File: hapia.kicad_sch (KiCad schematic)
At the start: 61 parts, among them CN1 100nf, CN2 100nf, J1 USB_C_Receptacle_USB2.0_16P, J18 Conn_ARM_JTAG_SWD_10, SW1 SW_Push, SW2 SW_Push, U1 AMS1117-3.3, U2 STM32F407VET6, U3 SRV05-4, Y1 8mhz

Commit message: 21082026/G
falta muita coisa
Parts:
- removed R10, R9: 33Ω, symbol Device:R
- removed R11: 1kΩ, symbol Device:R
- removed unit 2 of RN1
- removed unit 1 of RN1
- removed unit 6 of RN1
- removed unit 3 of RN1
- removed unit 5 of RN1
- removed unit 7 of RN1
- removed unit 4 of RN1
- removed unit 4 of RN2
- removed unit 1 of RN2
- removed unit 5 of RN2
- removed unit 6 of RN2
- removed unit 2 of RN2
- removed unit 3 of RN2
- removed unit 8 of RN2
- removed unit 3 of RN3
- removed unit 5 of RN3
- removed unit 7 of RN3
- removed unit 6 of RN3
- removed unit 1 of RN3
- removed unit 4 of RN3
- added R14, R15, R16, R17, R18, R19, R2, R20, R21, R22, R23, R24, R25, R26, R3, R30, R31, R32, R33, R34, R35, R36, R37, R38, R39, R40, R45, R46, R47, R5, R6, R7: 33Ω, symbol Device:R
- renumbered C16 to C10, C14 to C11, C17 to C12, C13 to C2, C2 to C3, C3 to C4, C11 to C5, C67 to C6, C4 to C7, C29 to C8, C5 to C9, D5 to D1, D1 to D2, FB2 to FB1, J18 to J1, J1 to J2, R43 to R1, R6 to R10, R24 to R11, R25 to R12, R4 to R13, R42 to R27, R23 to R28, R22 to R29, R3 to R4, R12 to R41, R13 to R42, R14 to R43, R5 to R44, R15 to R48, R16 to R49, R18 to R50, R19 to R51, R1 to R52, R20 to R53, R21 to R54, R7 to R9, RN3 to RN1, RN2 to RN1, RN1 to RN2, RN4 to RN3, RN5 to RN4, TP12 to TP1, TP16 to TP2, TP1 to TP3, TP2 to TP4, U2 to U1, U1 to U2
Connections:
- net Fan_1: now also R16.2; no longer R8.2
- net NTC_MUX_0: now also U1.55 (PD8); no longer U1.42 (PE11)
- net NTC_MUX_1: now also U1.56 (PD9); no longer U1.43 (PE12)
- net NTC_MUX_2: now also U1.57 (PD10); no longer U1.44 (PE13)
- net NTC_MUX_out: now also U1.15 (PC0); no longer U1.41 (PE10)
- net SUB_2: now also R33.2
- net SUB_3: now also R34.2
- net SUB_4: now also R35.2
- net SUB_5: now also R36.2
- net SUB_6: now also RN2.9 (R8.2)
- net SUB_SCL: now also R4.2
- net SUB_SDA: now also R5.2; no longer RN1.15 (R2.2)
- net SUB_led: now also R6.2; no longer RN2.9 (R8.2)
- net SWD_SWO: now also U1.35 (PB0); no longer U1.89 (PB3)
- net SWD/jtag_rst: now also U1.36 (PB1); no longer U1.90 (PB4)
- net TMC_DIR_3: now also R9.2; no longer RN4.3 (R3.1)
- net TMC_step_3: now also R10.2, R8.2; no longer RN4.2 (R2.1), RN4.4 (R4.1)
- net USB_C_D+: now also R26.2; no longer RN1.9 (R8.2)
- net USB_C_D-: now also R25.2; no longer RN1.10 (R7.2)
- net cont_sd: now also R7.2; no longer R4.2
- net exrtusora: now also R14.2; no longer R10.2
- net gpi_PD0: now also R45.2
- net gpi_PD1: now also R47.2
- net gpi_PD10: now also R24.2
- net gpi_PD11: now also R30.2
- net gpi_PD12: now also R31.2
- net gpi_PD13: now also R32.2
- net gpi_PD14: now also R2.2
- net gpi_PD15: now also R3.2
- net gpi_PD2: now also R46.2
- net gpi_PD3: now also R17.2
- net gpi_PD4: now also R18.2
- net gpi_PD5: now also R19.2
- net gpi_PD6: now also R20.2
- net gpi_PD7: now also R21.2
- net gpi_PD8: now also R22.2
- net gpi_PD9: now also R23.2
- net hot_bed: now also R15.2; no longer R9.2
- net at U1.82 (PD1): now also R18.1
- net at U1.81 (PD0): now also R17.1
- net at R13.1: now also U1.43 (PE12); no longer U1.40 (PE9)
- net at R43.1: now also U1.65 (PC8); no longer U1.80 (PC12)
- net at U1.91 (PB5): now also R32.1
- net at R8.1: now also U1.38 (PE7); no longer U1.37 (PB2)
- net at U1.86 (PD5): now also R22.1
- net at U1.64 (PC7): now also R42.1
- net at U1.93 (PB7): now also R34.1
- net at U1.1 (PE2): now also RN2.8 (R8.1)
- net at U1.17 (PC2): now also R39.1
- net at U1.18 (PC3): now also R40.1
- net at U1.2 (PE3): now also R4.1
- net at U1.3 (PE4): now also R5.1
- net at R10.1: now also U1.40 (PE9); no longer U1.35 (PB0)
- net at R9.1: now also U1.39 (PE8); no longer U1.36 (PB1)
- net at R11.1: now also U1.41 (PE10); no longer U1.38 (PE7)
- net at R12.1: now also U1.42 (PE11); no longer U1.39 (PE8)
- net at U1.4 (PE5): now also R6.1
- net at U1.45 (PE14): now also R15.1
- net at U1.46 (PE15): now also R16.1
- net at U1.5 (PE6): now also R7.1
- net at U1.51 (PB12): now also R37.1
- net at U1.52 (PB13): now also R38.1
- net at U1.61 (PD14): now also R25.1; no longer RN1.7 (R7.1)
- net at U1.62 (PD15): now also R26.1; no longer RN1.8 (R8.1)
- net at U1.63 (PC6): now also R41.1
- net at U1.66 (PC9): now also R44.1
- net at U1.77 (PA15): no longer R44.1
- net at U1.78 (PC10): now also R45.1; no longer R41.1
- net at U1.79 (PC11): now also R46.1; no longer R42.1
- net at U1.83 (PD2): now also R19.1
- net at U1.84 (PD3): now also R20.1
- net at U1.85 (PD4): now also R21.1
- net at U1.87 (PD6): now also R23.1
- net at U1.88 (PD7): now also R24.1
- net at U1.92 (PB6): now also R33.1
- net at U1.95 (PB8): now also R35.1
- net at U1.96 (PB9): now also R36.1
- net at U1.97 (PE0): now also R2.1; no longer RN2.8 (R8.1)
- net at U1.98 (PE1): now also R3.1; no longer R4.1
- new net: R30.1, U1.89 (PB3)
- new net: R14.1, U1.44 (PE13)
- new net: R47.1, U1.80 (PC12)
- new net: R31.1, U1.90 (PB4)
- new net SUB_GPIO_1: R39.2
- new net SUB_GPIO_2: R40.2
- new net SUB_RMII_CRS_DV: RN4.2 (R2.1)
- new net SUB_RMII_RXD0: RN4.3 (R3.1)
- new net SUB_RMII_RXD1: RN4.4 (R4.1)
- new net SUB_RMII_TXD0: R37.2
- new net SUB_RMII_TXD1: R38.2
- new net SUB_RMII_TXEN: RN1.15 (R2.2)
- no-connect marks 31 -> 23
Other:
- moved on the sheet: R10, R11, R12, R13, R4, R41, R42, R43, R44, R49, R8, R9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

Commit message: 23082026/H
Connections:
- net ATX_PWR_o: now reaches U1.47 (PB10)
- no-connect marks 23 -> 22
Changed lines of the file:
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@@
-	)
-	(no_connect
-		(at 128.27 163.83)
 	)
 	(no_connect
@@
 			(hide yes)
 			(show_name no)
+			(do_not_autoplace no)
+			(effects
+				(font
+					(size 1.27 1.27)
+				)
+				(justify left)
+			)
+		)
+	)
+	(global_label "ATX_PWR_o"
+		(shape input)
+		(at 128.27 163.83 0)
+		(fields_autoplaced yes)
+		(effects
+			(font
+				(size 1.27 1.27)
+			)
+			(justify left)
+		)
+		(property "Intersheetrefs" "${INTERSHEET_REFS}"
+			(at 141.5965 163.83 0)
+			(hide yes)
+			(show_name no)

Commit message: 29082026/I
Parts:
- removed R10, R11, R12, R13, R14, R15, R16, R17, R18, R19, R2, R20, R21, R22, R23, R24, R3, R36, R37, R38, R39, R4, R44, R45, R46, R47, R5, R6, R7, R8, R9: 33Ω, symbol Device:R
- removed R43: 33r, symbol Device:R
- removed unit 2 of RN1
- removed RN3, RN4: 33Ω, Resistor_SMD:R_Array_Convex_4x0603, symbol Device:R_Pack04_Split
- added R110, R111, R112, R113, R75: 33Ω, symbol Device:R
- added unit 4 of RN1
- added unit 6 of RN1
- added unit 3 of RN1
- added unit 5 of RN1
- added unit 4 of RN2
- added unit 6 of RN2
- added unit 1 of RN2
- added unit 2 of RN2
- added unit 3 of RN2
- added unit 7 of RN2
- added unit 5 of RN2
- added RN4: 33Ω, symbol Device:R_Pack08_Split
- added RN5, RN6: 33Ω, Resistor_SMD:R_Array_Concave_4x0402, symbol Device:R_Pack04_Split
- C10: footprint (none) -> Capacitor_SMD:C_0603_1608Metric; jlc_pcb: (none) -> C162274; mouser: (none) -> 81-GRM188R61E475KE1D; mpn (none) -> GRM188R61E475KE11D
- C11, C2: footprint (none) -> Capacitor_SMD:C_1206_3216Metric_Pad1.33x1.80mm_HandSolder; jlc_pcb: (none) -> C13585; mouser: (none) -> 187-CL31B106KLK6PNE; mpn (none) -> CL31A106KBHNNNE
- C3, C4, C7, C9: jlc_pcb: C346191 -> C307348; mouser: (none) -> 187-CL10B104KB8WPNC; mpn CL10B104KB8NFNC -> CL10B104KB8WPNC
- C6: footprint (none) -> Capacitor_SMD:C_1206_3216Metric_Pad1.33x1.80mm_HandSolder; Descrição (none) -> esse capacitor e conectado entre o gnd e o vcc(VDDA) do ci 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; jlc_pcb: (none) -> C13585; mouser: (none) -> 187-CL31B106KLK6PNE; mpn (none) -> CL31A106KBHNNNE
- C8: footprint (none) -> Capacitor_SMD:C_0603_1608Metric; Descrição (none) -> capacitor ceramico 4.7uf(µf); jlc_pcb: (none) -> C162274; mouser: (none) -> 81-GRM188R61E475KE1D; mpn (none) -> GRM188R61E475KE11D
- CN1, CN2: jlc_pcb: C346191 -> C307348; mouser: (none) -> 187-CL10B104KB8WPNC; mpn CA0612MRX7R7BB104 -> CL10B104KB8WPNC
- J2: footprint (none) -> Connector_USB:USB_C_Receptacle_HCTL_HC-TYPE-C-16P-01A; jlc_pcb: (none) -> C5150972; mouser: (none) -> 523-12402012E212A; mpn (none) -> 12402012E212A
- R25, R26: value 33Ω -> 22Ω
- R41, R42: value 33r -> 33Ω
- R48: value 1k -> 1kΩ
- RN1, RN2: footprint Resistor_SMD:R_Array_Convex_8x0602 -> (none)
- U1: mouser: (none) -> 511-STM32F407VET6
- U2: mouser: (none) -> 926-LM1117MPX3.3NOPB
- Y1: mouser: (none) -> 815-ABM3-8-D2Y-T
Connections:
- net ATX_PWR_o: now also RN1.8 (R8.1); no longer U1.47 (PB10)
- net Fan_1: now also RN6.5 (R4.2)
- net Fan_2: now also RN6.8 (R1.2)
- net SDW_SWCLK: now also R41.2; no longer R29.2
- net SDW_SWDIO: now also R40.2; no longer R28.2
- net SUB_2: now also RN1.6 (R6.1); no longer R33.2
- net SUB_3: now also RN1.5 (R5.1); no longer R34.2
- net SUB_4: now also RN1.4 (R4.1); no longer R35.2
- net SUB_5: now also RN1.3 (R3.1)
- net SUB_6: now also U1.1 (PE2); no longer RN2.9 (R8.2)
- net SUB_GPIO_1: now also RN4.1 (R1.1)
- net SUB_GPIO_2: now also RN4.2 (R2.1); no longer R40.2
- net SUB_RMII_CRS_DV: now also U1.32 (PA7)
- net SUB_RMII_RXD0: now also RN4.3 (R3.1)
- net SUB_RMII_RXD1: now also RN4.4 (R4.1)
- net SUB_RMII_TXD0: now also R30.2
- net SUB_RMII_TXD1: now also R31.2
- net SUB_RMII_TXEN: now also R29.2
- net SUB_SCL: now also U1.2 (PE3)
- net SUB_SDA: now also U1.3 (PE4)
- net SUB_led: now also U1.4 (PE5)
- net TMC_DIR_1: now also R75.2
- net TMC_DIR_2: now also R111.2
- net TMC_DIR_3: now also R113.2, RN5.7 (R2.2)
- net TMC_DIR_4: now also R42.2
- net TMC_step_1: now also R110.2
- net TMC_step_2: now also R112.2
- net TMC_step_3: now also RN5.6 (R3.2), RN5.8 (R1.2)
- net TMC_step_4: now also RN5.5 (R4.2)
- net cont_sd: now also U1.5 (PE6)
- net exrtusora: now also RN6.7 (R2.2)
- net gpi_PD0: now also R34.2
- net gpi_PD1: now also RN2.1 (R1.1)
- net gpi_PD10: now also R28.2
- net gpi_PD11: now also R32.2; no longer R30.2
- net gpi_PD12: now also R33.2; no longer R31.2
- net gpi_PD13: now also RN1.7 (R7.1); no longer R32.2
- net gpi_PD14: now also U1.70 (PA11)
- net gpi_PD15: now also U1.71 (PA12)
- net gpi_PD2: now also R35.2
- net gpi_PD3: now also RN2.2 (R2.1)
- net gpi_PD4: now also RN2.3 (R3.1)
- net gpi_PD5: now also RN2.4 (R4.1)
- net gpi_PD6: now also RN2.5 (R5.1)
- net gpi_PD7: now also RN2.6 (R6.1)
- net gpi_PD8: now also RN2.7 (R7.1)
- net gpi_PD9: now also RN2.8 (R8.1)
- net hot_bed: now also RN6.6 (R3.2)
- net sd_SCK: now also RN4.5 (R5.1); no longer R41.2
- net sd_cs: now also RN4.8 (R8.1)
- net sd_miso: now also RN4.6 (R6.1); no longer R42.2
- net sd_mosi: now also RN4.7 (R7.1)
- net at U1.52 (PB13): now also R31.1
- net at U1.43 (PE12): now also RN6.1 (R1.1)
- net at U1.65 (PC8): now also RN4.10 (R7.2)
- net at U1.79 (PC11): now also R35.1
- net at U1.38 (PE7): now also RN5.1 (R1.1)
- net at U1.48 (PB11): now also R29.1
- net at U1.85 (PD4): now also RN2.11 (R6.2)
- net at U1.18 (PC3): now also RN4.15 (R2.2); no longer R40.1
- net at U1.26 (PA3): now also R110.1
- net at U1.51 (PB12): now also R30.1
- net at U1.89 (PB3): now also R32.1; no longer R30.1
- net at U1.88 (PD7): now also R28.1
- net at R48.1: now also U1.24 (PA1); no longer U1.23 (PA0)
- net at R48.2, R49.1: now also U1.23 (PA0); no longer U1.24 (PA1)
- net at U1.17 (PC2): now also RN4.16 (R1.2)
- net at U1.25 (PA2): now also R75.1
- net at U1.29 (PA4): now also R111.1
- net at U1.30 (PA5): now also R112.1
- net at U1.31 (PA6): now also R113.1
- net at U1.33 (PC4): now also RN4.14 (R3.2)
- net at U1.34 (PC5): now also RN4.13 (R4.2)
- net at U1.39 (PE8): now also RN5.2 (R2.1)
- net at U1.40 (PE9): now also RN5.3 (R3.1)
- net at U1.41 (PE10): now also RN5.4 (R4.1)
- net at U1.42 (PE11): now also R42.1
- net at U1.44 (PE13): now also RN6.2 (R2.1)
- net at U1.45 (PE14): now also RN6.3 (R3.1)
- net at U1.46 (PE15): now also RN6.4 (R4.1)
- net at R41.1: now also U1.76 (PA14); no longer U1.63 (PC6)
- net at U1.64 (PC7): now also RN4.11 (R6.2); no longer R42.1
- net at U1.66 (PC9): now also RN4.9 (R8.2)
- net at U1.72 (PA13): now also R40.1; no longer R28.1
- net at U1.78 (PC10): now also R34.1
- net at U1.80 (PC12): now also RN2.16 (R1.2)
- net at U1.81 (PD0): now also RN2.15 (R2.2)
- net at U1.82 (PD1): now also RN2.14 (R3.2)
- net at U1.83 (PD2): now also RN2.13 (R4.2)
- net at U1.84 (PD3): now also RN2.12 (R5.2)
- net at U1.86 (PD5): now also RN2.10 (R7.2)
- net at U1.87 (PD6): now also RN2.9 (R8.2)
- net at U1.90 (PB4): now also R33.1; no longer R31.1
- net at U1.91 (PB5): now also RN1.10 (R7.2); no longer R32.1
- net at U1.92 (PB6): now also RN1.11 (R6.2); no longer R33.1
- net at U1.93 (PB7): now also RN1.12 (R5.2); no longer R34.1
- net at U1.95 (PB8): now also RN1.13 (R4.2); no longer R35.1
- net at U1.96 (PB9): now also RN1.14 (R3.2)
- net at U1.97 (PE0): now also RN1.9 (R8.2)
- net MUX_EN: now reaches U1.98 (PE1)
- new net: RN4.12 (R5.2), U1.63 (PC6)
- no-connect marks 22 -> 21
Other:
- moved on the sheet: R48

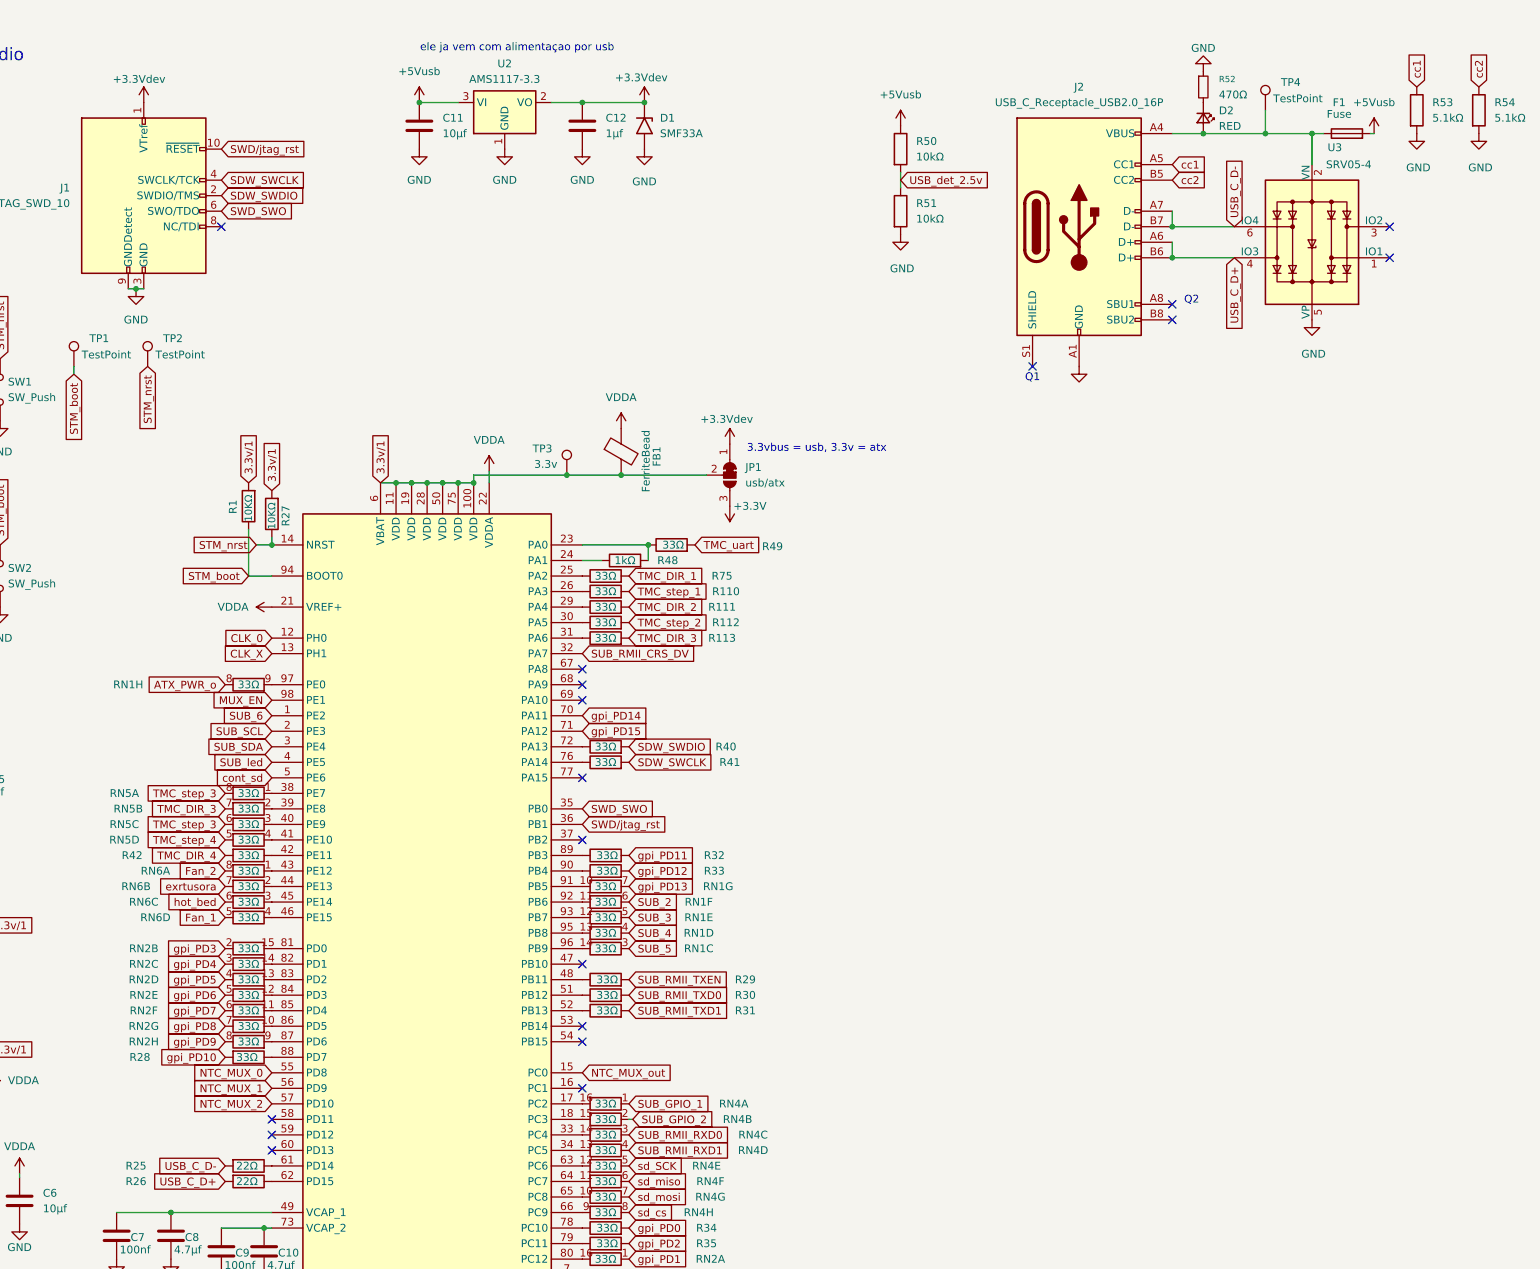
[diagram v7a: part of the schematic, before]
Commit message: o .bom não foi terminado
O desafio e todo custar menos de 150 dólares(eua) e menos de 1000r(reais)
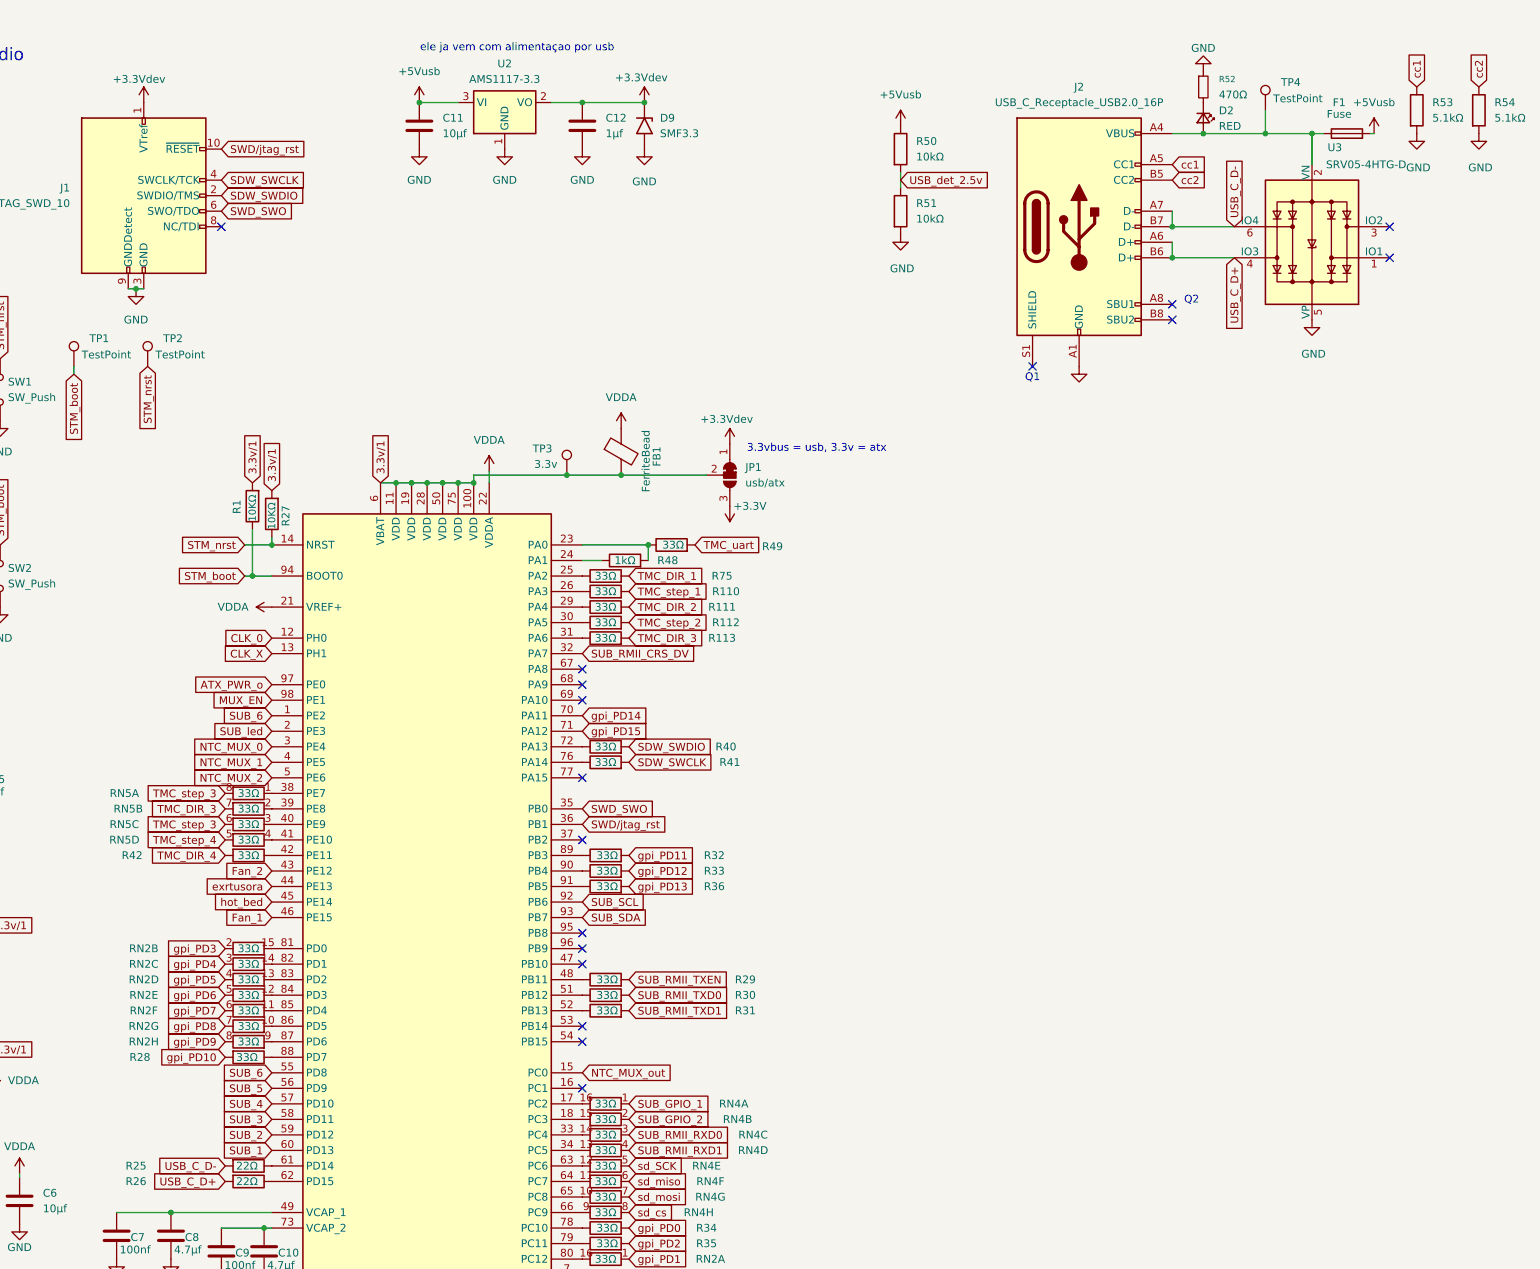
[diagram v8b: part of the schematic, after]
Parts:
- removed D1: SMF33A, Diode_SMD:D_SMF, symbol Diode:SMF33A
- removed RN1: 33Ω, symbol Device:R_Pack08_Split
- removed RN6: 33Ω, Resistor_SMD:R_Array_Concave_4x0402, symbol Device:R_Pack04_Split
- added D9: SMF3.3, Diode_SMD:D_SMF, symbol Diode:SMF5V0A
- added R36: 33Ω, Resistor_SMD:R_0603_1608Metric_Pad0.98x0.95mm_HandSolder, symbol Device:R
- C1, C5: mouser: (none) -> 80-C0603C220J4G
- C10, C8: footprint Capacitor_SMD:C_0603_1608Metric -> Capacitor_SMD:C_0603_1608Metric_Pad1.08x0.95mm_HandSolder
- C12: mouser: (none) -> 187-CL21B105KBFNNNE; mpn (none) -> CL21B105KBFNNNE
- R110, R111, R112, R113, R28, R29, R30, R31, R32, R33, R34, R35, R40, R41, R42, R49, R75: footprint (none) -> Resistor_SMD:R_0603_1608Metric_Pad0.98x0.95mm_HandSolder; jlc_pcb: (none) -> C844927; mouser: (none) -> 71-CRCW0603-33-E3; mpn (none) -> CRCW060333R0FKEA
- R25, R26: footprint (none) -> Resistor_SMD:R_0603_1608Metric_Pad0.98x0.95mm_HandSolder; jlc_pcb: (none) -> C71618; mouser: (none) -> 71-CRCW0603-22-E3; mpn (none) -> CRCW060322R0FKEA
- RN2, RN4: footprint (none) -> Resistor_SMD:R_Array_Concave_4x0402; jlc_pcb: (none) -> C148513; mouser: (none) -> 652-CAT10-330J4LF; mpn (none) -> CAT10-330J4LF
- RN5: mouser: (none) -> 652-CAT10-330J4LF
- SW1, SW2: footprint (none) -> Connector_PinHeader_2.54mm:PinHeader_1x02_P2.54mm_Vertical; jlc_pcb: (none) -> C234182; mouser: (none) -> 538-22-28-4020; mpn (none) -> 22284020
- TP1, TP2, TP3, TP4: now left out of the parts list
- U3: value SRV05-4 -> SRV05-4HTG-D; jlc_pcb: ssss -> C1975211; mouser: (none) -> 576-SRV05-4HTG-D; mpn ssss -> SRV05-4HTG-D
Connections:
- net cont_sd is gone; now on net NTC_MUX_2: U1.5 (PE6)
- net +3.3Vdev: now also D9.1 (A1)
- net ATX_PWR_o: now also U1.97 (PE0)
- net Fan_1: now also U1.46 (PE15)
- net Fan_2: now also U1.43 (PE12)
- net GND: now also D9.2 (A2)
- net NTC_MUX_0: now also U1.3 (PE4); no longer U1.55 (PD8)
- net NTC_MUX_1: now also U1.4 (PE5); no longer U1.56 (PD9)
- net NTC_MUX_2: no longer U1.57 (PD10)
- net SUB_2: now also U1.59 (PD12)
- net SUB_3: now also U1.58 (PD11)
- net SUB_4: now also U1.57 (PD10)
- net SUB_5: now also U1.56 (PD9)
- net SUB_6: now also U1.55 (PD8)
- net SUB_SCL: now also U1.92 (PB6); no longer U1.2 (PE3)
- net SUB_SDA: now also U1.93 (PB7); no longer U1.3 (PE4)
- net SUB_led: now also U1.2 (PE3); no longer U1.4 (PE5)
- net exrtusora: now also U1.44 (PE13)
- net gpi_PD13: now also R36.2
- net hot_bed: now also U1.45 (PE14)
- net SUB_1: now reaches U1.60 (PD13)
- net at U1.91 (PB5): now also R36.1
- no-connect marks 21 -> 20
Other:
- moved on the sheet: R1
